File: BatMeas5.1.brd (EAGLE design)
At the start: 65.1 x 34.3 mm, 48 parts, among them IC1 ATTINY24, IC2 3V3, IC3 3V, T1 MMUN2233, T2 MMUN2233, T3 MMUN2233, T4 MMUN2111LT1G, T5 MMUN2111LT1G, T6 MMUN2111LT1G, T7 MMUN2233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

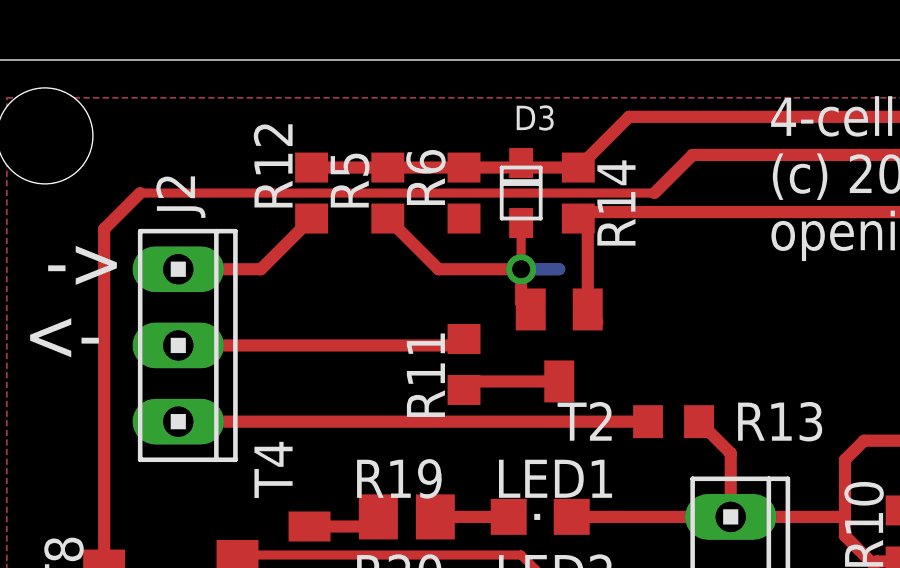
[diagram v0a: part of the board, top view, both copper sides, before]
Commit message: Fixed dangling pin of R6
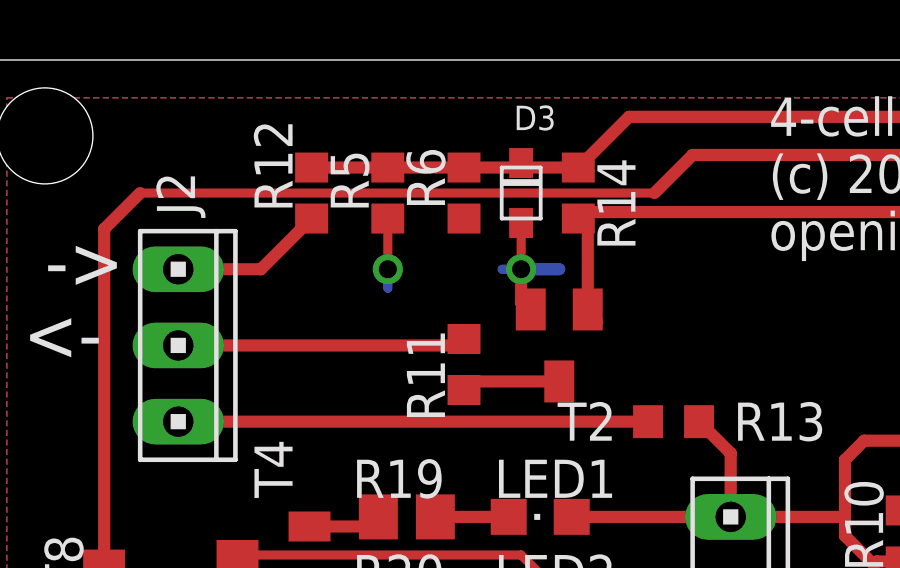
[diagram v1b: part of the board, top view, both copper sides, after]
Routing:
- net GND: track 76.4 -> 73.6 mm, vias 11 -> 12
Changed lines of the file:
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@@
 <wire x1="39.37" y1="16.5401" x2="39.37" y2="17.565" width="0.4064" layer="1"/>
 <contactref element="R5" pad="1"/>
-<wire x1="13.97" y1="28.995" x2="15.66" y2="27.305" width="0.4064" layer="1"/>
-<wire x1="15.66" y1="27.305" x2="18.415" y2="27.305" width="0.4064" layer="1"/>
-<wire x1="55.245" y1="25.4" x2="55.245" y2="27.94" width="0" layer="19" extent="1-1"/>
-<wire x1="55.245" y1="22.86" x2="55.245" y2="25.4" width="0" layer="19" extent="1-1"/>
-<wire x1="55.245" y1="20.32" x2="55.245" y2="22.86" width="0" layer="19" extent="1-1"/>
-<wire x1="47.625" y1="22.8299" x2="55.245" y2="22.86" width="0" layer="19" extent="1-1"/>
-<wire x1="40.005" y1="17.78" x2="39.37" y2="19.685" width="0" layer="19" extent="1-16"/>
-<wire x1="37.465" y1="12.7" x2="36.195" y2="15.455" width="0" layer="19" extent="1-16"/>
-<wire x1="37.465" y1="8.89" x2="37.465" y2="11.43" width="0" layer="19" extent="16-16"/>
-<wire x1="40.64" y1="26.33" x2="38.735" y2="20.32" width="0" layer="19" extent="1-1"/>
-<wire x1="45.72" y1="6.985" x2="38.735" y2="8.89" width="0" layer="19" extent="16-16"/>
-<wire x1="25.4" y1="8.89" x2="33.655" y2="7.835" width="0" layer="19" extent="1-1"/>
-<wire x1="19.05" y1="7.62" x2="25.4" y2="8.89" width="0" layer="19" extent="16-16"/>
-<wire x1="61.595" y1="13.12" x2="55.245" y2="20.32" width="0" layer="19" extent="1-1"/>
-<wire x1="4.515" y1="9.21" x2="15.805" y2="7.935" width="0" layer="19" extent="1-1"/>
-<wire x1="4.515" y1="12.385" x2="4.515" y2="9.21" width="0" layer="19" extent="1-1"/>
-<wire x1="15.66" y1="27.305" x2="5.395" y2="15.56" width="0" layer="19" extent="1-1"/>
+<wire x1="13.97" y1="28.995" x2="13.97" y2="27.305" width="0.3048" layer="1"/>
+<via x="13.97" y="27.305" extent="1-16" drill="0.6" shape="octagon"/>
+<wire x1="13.97" y1="27.305" x2="13.97" y2="26.67" width="0.3048" layer="16"/>
 </signal>
 <signal name="VCC">
